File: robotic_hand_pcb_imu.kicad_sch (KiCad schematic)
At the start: 13 parts, among them U7 BNO085, Y3 32k768

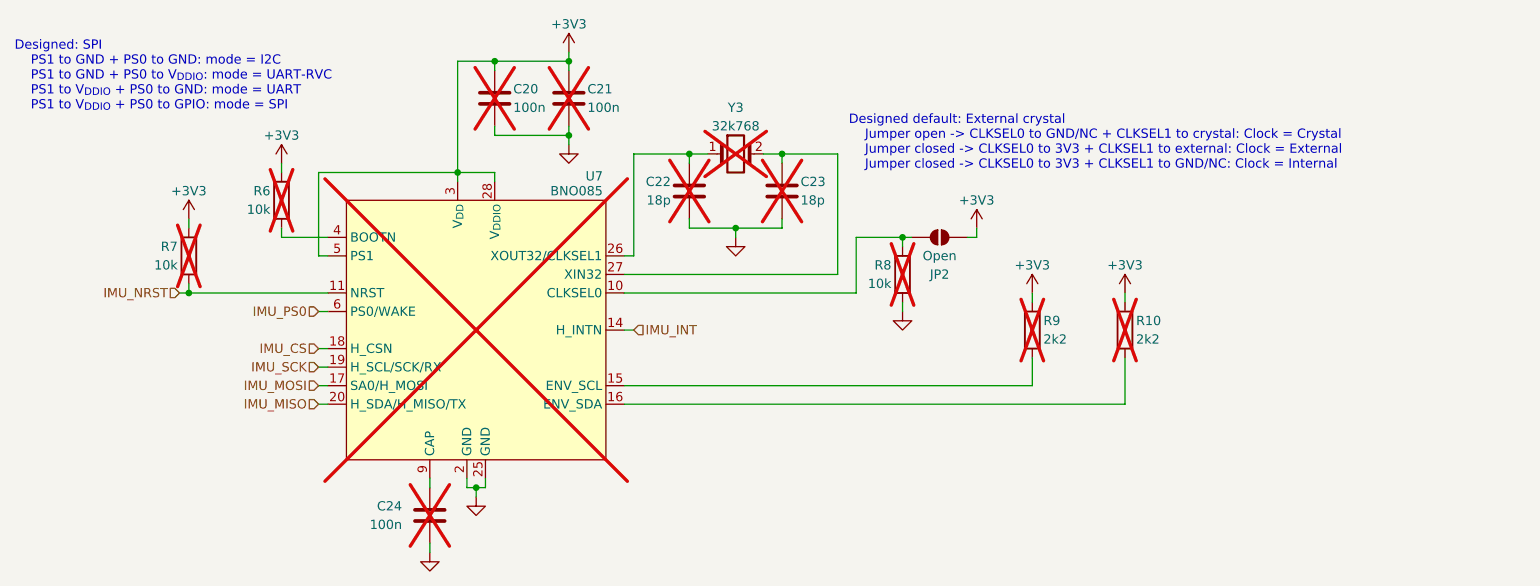
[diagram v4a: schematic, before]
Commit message: Add WIP PCB layout and routing
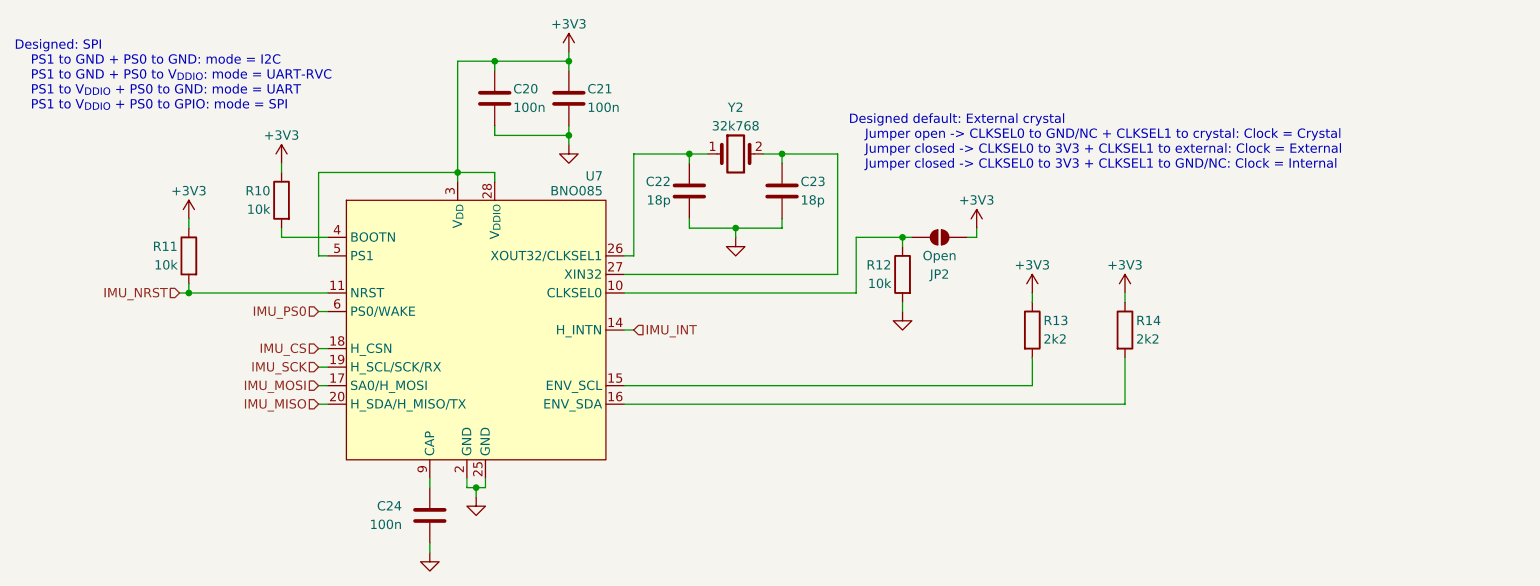
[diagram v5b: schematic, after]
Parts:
- C20, C21, C22, C23, C24, U7: now fitted
- R10: renamed from R6; now fitted
- R11: renamed from R7; now fitted
- R12: renamed from R8; now fitted
- R13: renamed from R9; now fitted
- R14: renamed from R10; now fitted
- Y2: renamed from Y3; now fitted
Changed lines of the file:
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@@
 		(on_board yes)
 		(dnp no)
-		(property "Reference" "#PWR047"
+		(property "Reference" "#PWR048"
 			(at 182.88 67.31 0)
 			(effects
@@
 			(project "robotic_hand_pcb"
 				(path "/96df9010-a1f8-4419-aac0-9388de87cb21/f209e5e9-1726-454a-82e1-5fd492ecf1c3"
-					(reference "#PWR047")
+					(reference "#PWR048")
 					(unit 1)
 				)
@@
 		(in_bom yes)
 		(on_board yes)
-		(dnp yes)
+		(dnp no)
 		(property "Reference" "C22"
 			(at 120.65 48.26 0)
@@
 		(in_bom yes)
 		(on_board yes)
-		(dnp yes)
-		(property "Reference" "R9"
+		(dnp no)
+		(property "Reference" "R13"
 			(at 171.704 67.31 0)
 			(effects
@@
 			(project "robotic_hand_pcb"
 				(path "/96df9010-a1f8-4419-aac0-9388de87cb21/f209e5e9-1726-454a-82e1-5fd492ecf1c3"
-					(reference "R9")
+					(reference "R13")
 					(unit 1)
 				)
@@
 		(dnp no)
 		(fields_autoplaced yes)
-		(property "Reference" "#PWR050"
+		(property "Reference" "#PWR051"
 			(at 87.63 105.41 0)
 			(effects
@@
 			(project "robotic_hand_pcb"
 				(path "/96df9010-a1f8-4419-aac0-9388de87cb21/f209e5e9-1726-454a-82e1-5fd492ecf1c3"
-					(reference "#PWR050")
+					(reference "#PWR051")
 					(unit 1)
 				)
@@
 		(in_bom yes)
 		(on_board yes)
-		(dnp yes)
-		(property "Reference" "R7"
+		(dnp no)
+		(property "Reference" "R11"
 			(at 53.086 57.15 0)
 			(effects
@@
 			(project "robotic_hand_pcb"
 				(path "/96df9010-a1f8-4419-aac0-9388de87cb21/f209e5e9-1726-454a-82e1-5fd492ecf1c3"
-					(reference "R7")
+					(reference "R11")
 					(unit 1)
 				)
@@
 		(on_board yes)
 		(dnp no)
-		(property "Reference" "#PWR044"
+		(property "Reference" "#PWR045"
 			(at 162.56 58.42 0)
 			(effects
@@
 			(project "robotic_hand_pcb"
 				(path "/96df9010-a1f8-4419-aac0-9388de87cb21/f209e5e9-1726-454a-82e1-5fd492ecf1c3"
-					(reference "#PWR044")
+					(reference "#PWR045")
 					(unit 1)
 				)
@@
 		(dnp no)
 		(fields_autoplaced yes)
-		(property "Reference" "#PWR041"
+		(property "Reference" "#PWR042"
 			(at 106.68 49.53 0)
 			(effects
@@
 			(project "robotic_hand_pcb"
 				(path "/96df9010-a1f8-4419-aac0-9388de87cb21/f209e5e9-1726-454a-82e1-5fd492ecf1c3"
-					(reference "#PWR041")
+					(reference "#PWR042")
 					(unit 1)
 				)
@@
 		(on_board yes)
 		(dnp no)
-		(property "Reference" "#PWR042"
+		(property "Reference" "#PWR043"
 			(at 67.31 49.53 0)
 			(effects
@@
 			(project "robotic_hand_pcb"
 				(path "/96df9010-a1f8-4419-aac0-9388de87cb21/f209e5e9-1726-454a-82e1-5fd492ecf1c3"
-					(reference "#PWR042")
+					(reference "#PWR043")
 					(unit 1)
 				)
@@
 		(dnp no)
 		(fields_autoplaced yes)
-		(property "Reference" "#PWR049"
+		(property "Reference" "#PWR050"
 			(at 93.98 97.79 0)
 			(effects
@@
 			(project "robotic_hand_pcb"
 				(path "/96df9010-a1f8-4419-aac0-9388de87cb21/f209e5e9-1726-454a-82e1-5fd492ecf1c3"
-					(reference "#PWR049")
+					(reference "#PWR050")
 					(unit 1)
 				)
@@
 		(in_bom yes)
 		(on_board yes)
-		(dnp yes)
+		(dnp no)
 		(property "Reference" "C23"
 			(at 138.43 48.26 0)
@@
 		(in_bom yes)
 		(on_board yes)
-		(dnp yes)
-		(property "Reference" "R8"
+		(dnp no)
+		(property "Reference" "R12"
 			(at 150.876 59.69 0)
 			(effects
@@
 			(project "robotic_hand_pcb"
 				(path "/96df9010-a1f8-4419-aac0-9388de87cb21/f209e5e9-1726-454a-82e1-5fd492ecf1c3"
-					(reference "R8")
+					(reference "R12")
 					(unit 1)
 				)
@@
 		(dnp no)
 		(fields_autoplaced yes)
-		(property "Reference" "#PWR045"
+		(property "Reference" "#PWR046"
 			(at 129.54 62.23 0)
 			(effects
@@
 			(project "robotic_hand_pcb"
 				(path "/96df9010-a1f8-4419-aac0-9388de87cb21/f209e5e9-1726-454a-82e1-5fd492ecf1c3"
-					(reference "#PWR045")
+					(reference "#PWR046")
 					(unit 1)
 				)
@@
 		(in_bom yes)
 		(on_board yes)
-		(dnp yes)
+		(dnp no)
 		(property "Reference" "C21"
 			(at 109.22 35.56 0)
@@
 		(at 93.98 68.58 0)
 		(unit 1)
-		(exclude_from_sim yes)
-		(in_bom yes)
-		(on_board yes)
-		(dnp yes)
+		(exclude_from_sim no)
+		(in_bom yes)
+		(on_board yes)
+		(dnp no)
 		(property "Reference" "U7"
 			(at 108.966 47.498 0)
@@
 		(on_board yes)
 		(dnp no)
-		(property "Reference" "#PWR040"
+		(property "Reference" "#PWR041"
 			(at 106.68 34.29 0)
 			(effects
@@
 			(project "robotic_hand_pcb"
 				(path "/96df9010-a1f8-4419-aac0-9388de87cb21/f209e5e9-1726-454a-82e1-5fd492ecf1c3"
-					(reference "#PWR040")
+					(reference "#PWR041")
 					(unit 1)
 				)
@@
 		(dnp no)
 		(fields_autoplaced yes)
-		(property "Reference" "#PWR048"
+		(property "Reference" "#PWR049"
 			(at 152.4 72.39 0)
 			(effects
@@
 			(project "robotic_hand_pcb"
 				(path "/96df9010-a1f8-4419-aac0-9388de87cb21/f209e5e9-1726-454a-82e1-5fd492ecf1c3"
-					(reference "#PWR048")
+					(reference "#PWR049")
 					(unit 1)
 				)
@@
 		(in_bom yes)
 		(on_board yes)
-		(dnp yes)
+		(dnp no)
 		(property "Reference" "C20"
 			(at 99.06 35.56 0)
@@
 		(on_board yes)
 		(dnp no)
-		(property "Reference" "#PWR046"
+		(property "Reference" "#PWR047"
 			(at 170.18 67.31 0)
 			(effects
@@
 			(project "robotic_hand_pcb"
 				(path "/96df9010-a1f8-4419-aac0-9388de87cb21/f209e5e9-1726-454a-82e1-5fd492ecf1c3"
-					(reference "#PWR046")
+					(reference "#PWR047")
 					(unit 1)
 				)
@@
 		(in_bom yes)
 		(on_board yes)
-		(dnp yes)
-		(property "Reference" "R6"
+		(dnp no)
+		(property "Reference" "R10"
 			(at 65.786 49.53 0)
 			(effects
@@
 			(project "robotic_hand_pcb"
 				(path "/96df9010-a1f8-4419-aac0-9388de87cb21/f209e5e9-1726-454a-82e1-5fd492ecf1c3"
-					(reference "R6")
+					(reference "R10")
 					(unit 1)
 				)
@@
 		(in_bom yes)
 		(on_board yes)
-		(dnp yes)
-		(property "Reference" "Y3"
+		(dnp no)
+		(property "Reference" "Y2"
 			(at 129.54 38.1 0)
 			(effects
@@
 			(project "robotic_hand_pcb"
 				(path "/96df9010-a1f8-4419-aac0-9388de87cb21/f209e5e9-1726-454a-82e1-5fd492ecf1c3"
-					(reference "Y3")
+					(reference "Y2")
 					(unit 1)
 				)
@@
 		(on_board yes)
 		(dnp no)
-		(property "Reference" "#PWR043"
+		(property "Reference" "#PWR044"
 			(at 54.61 57.15 0)
 			(effects
@@
 			(project "robotic_hand_pcb"
 				(path "/96df9010-a1f8-4419-aac0-9388de87cb21/f209e5e9-1726-454a-82e1-5fd492ecf1c3"
-					(reference "#PWR043")
+					(reference "#PWR044")
 					(unit 1)
 				)
@@
 		(in_bom yes)
 		(on_board yes)
-		(dnp yes)
-		(property "Reference" "R10"
+		(dnp no)
+		(property "Reference" "R14"
 			(at 184.404 67.31 0)
 			(effects
@@
 			(project "robotic_hand_pcb"
 				(path "/96df9010-a1f8-4419-aac0-9388de87cb21/f209e5e9-1726-454a-82e1-5fd492ecf1c3"
-					(reference "R10")
+					(reference "R14")
 					(unit 1)
 				)
@@
 		(in_bom yes)
 		(on_board yes)
-		(dnp yes)
+		(dnp no)
 		(property "Reference" "C24"
 			(at 83.82 92.7099 0)
